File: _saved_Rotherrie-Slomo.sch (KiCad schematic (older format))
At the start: 5 parts, among them J1 CONN_02X05

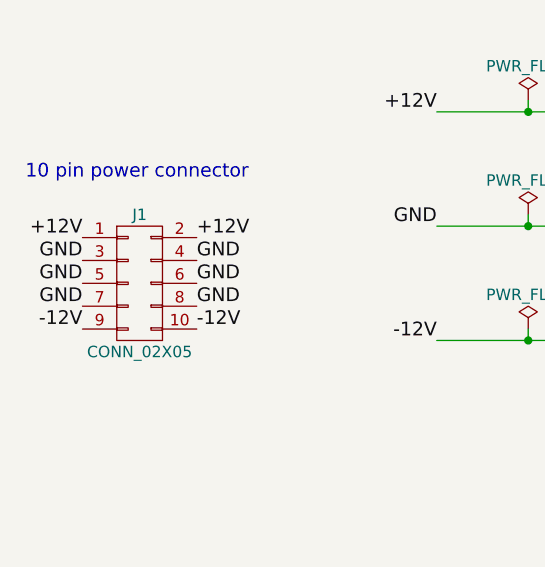
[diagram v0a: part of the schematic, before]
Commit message: Part associations made. 16pin connector reduced to 10 pin
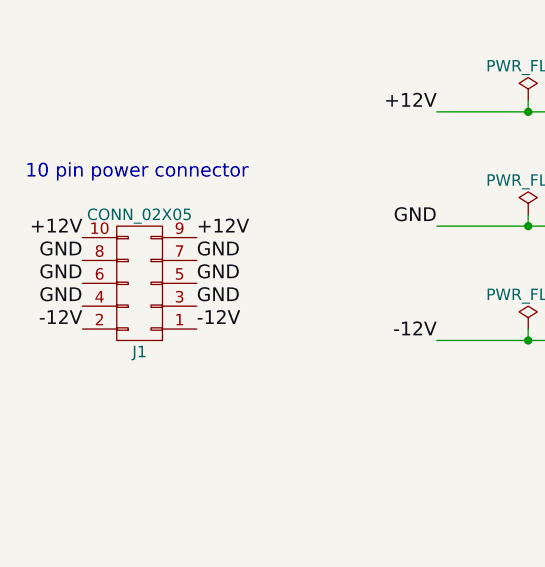
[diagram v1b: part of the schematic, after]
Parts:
- D1, D2: footprint (none) -> Diodes_THT:D_DO-41_SOD81_P7.62mm_Horizontal
- J1: footprint (none) -> Pin_Headers:Pin_Header_Straight_2x05_Pitch2.54mm
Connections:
- net VCC: now also J1.10 (P10), J1.9 (P9); no longer J1.1 (P1), J1.2 (P2)
- net VEE: now also J1.1 (P1), J1.2 (P2); no longer J1.10 (P10), J1.9 (P9)
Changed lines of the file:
@@
 F 0 "D1" H 4000 2350 50  0000 C CNN
 F 1 "1N5817" H 4000 2150 50  0000 C CNN
-F 2 "" H 4000 2250 50  0001 C CNN
+F 2 "Diodes_THT:D_DO-41_SOD81_P7.62mm_Horizontal" H 4000 2250 50  0001 C CNN
 F 3 "" H 4000 2250 50  0001 C CNN
 	1    4000 2250
@@
 F 0 "D2" H 4000 2850 50  0000 C CNN
 F 1 "1N5817" H 4000 2650 50  0000 C CNN
-F 2 "" H 4000 2750 50  0001 C CNN
+F 2 "Diodes_THT:D_DO-41_SOD81_P7.62mm_Horizontal" H 4000 2750 50  0001 C CNN
 F 3 "" H 4000 2750 50  0001 C CNN
 	1    4000 2750
@@
 F 0 "J1" H 1800 3050 50  0000 C CNN
 F 1 "CONN_02X05" H 1800 2450 50  0000 C CNN
-F 2 "" H 1800 1550 50  0001 C CNN
+F 2 "Pin_Headers:Pin_Header_Straight_2x05_Pitch2.54mm" H 1800 1550 50  0001 C CNN
 F 3 "" H 1800 1550 50  0001 C CNN
 	1    1800 2750
-	1    0    0    -1
+	-1   0    0    1
 $EndComp
 $EndSCHEMATC
